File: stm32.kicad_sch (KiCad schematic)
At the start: 19 parts, among them IC1 STM32L051C6T6, J6 702472054, SW1 PTS 647 SN50 SMTR2 LFS, SW2 SW_SPDT, Y1 8MHz, Y2 ABS25-32.768KHZ-6-T

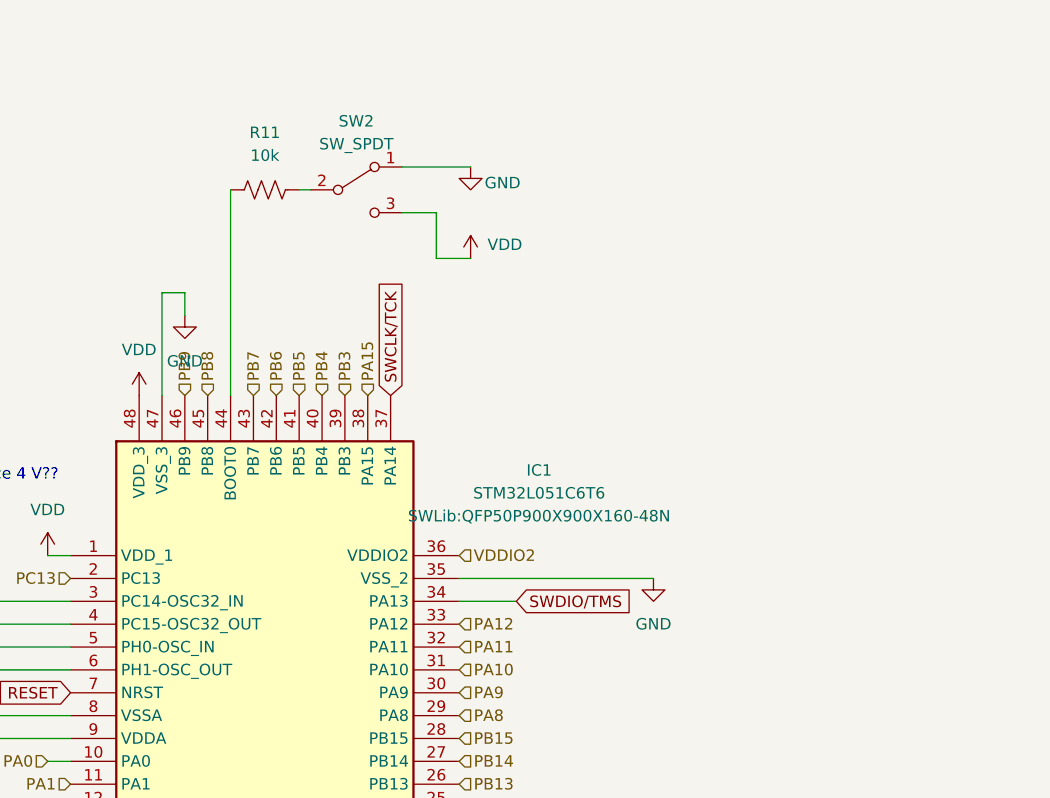
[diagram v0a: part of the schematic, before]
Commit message: removed msp430 and moved stm32, disconnected swdio and swclk in subsheet
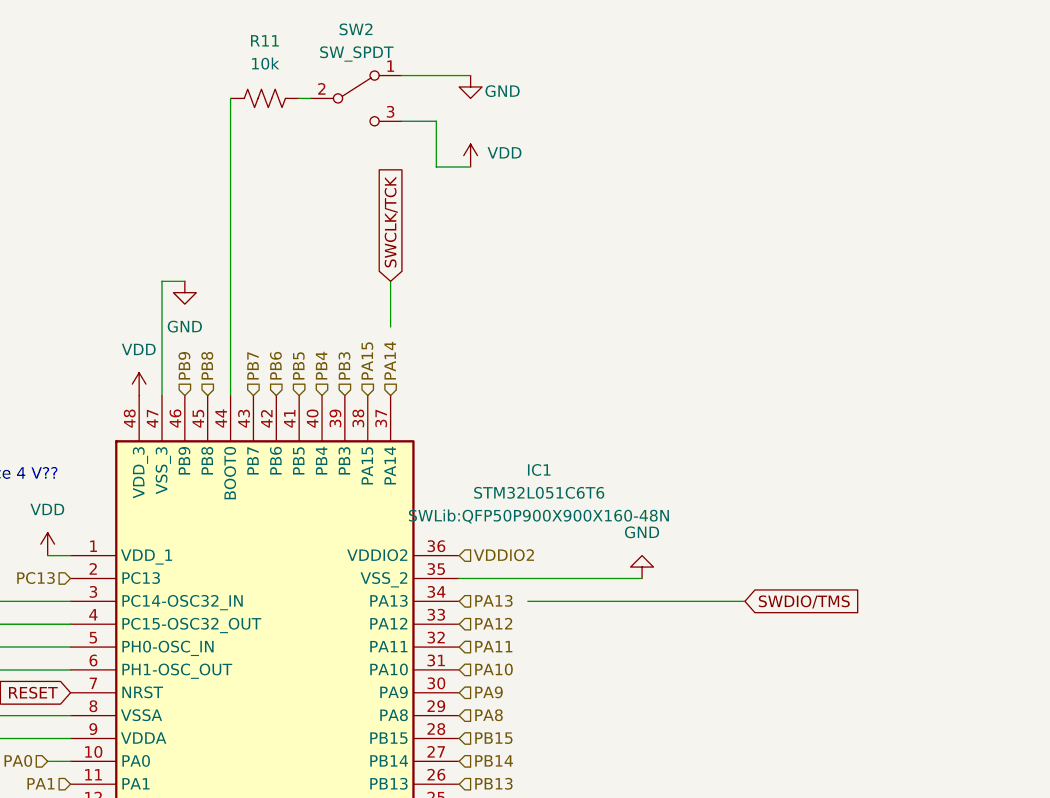
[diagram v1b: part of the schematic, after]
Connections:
- net SWCLK/TCK: no longer IC1.37 (PA14)
- net SWDIO/TMS: no longer IC1.34 (PA13)
- new net PA13: IC1.34 (PA13)
- new net PA14: IC1.37 (PA14)
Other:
- moved on the sheet: R11, SW2
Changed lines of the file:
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@@
 	(wire
 		(pts
-			(xy 147.32 44.45) (xy 149.86 44.45)
+			(xy 147.32 43.18) (xy 149.86 43.18)
 		)
 		(stroke
@@
 	(wire
 		(pts
+			(xy 172.72 43.18) (xy 172.72 48.26)
+		)
+		(stroke
+			(width 0)
+			(type default)
+		)
+	)
+	(wire
+		(pts
 			(xy 107.95 142.24) (xy 107.95 137.16)
 		)
@@
 	(wire
 		(pts
+			(xy 187.96 78.74) (xy 212.09 78.74)
+		)
+		(stroke
+			(width 0)
+			(type default)
+		)
+	)
+	(wire
+		(pts
 			(xy 105.41 149.86) (xy 105.41 154.94)
 		)
@@
 	(wire
 		(pts
-			(xy 154.94 33.02) (xy 154.94 55.88)
+			(xy 154.94 22.86) (xy 154.94 55.88)
 		)
 		(stroke
@@
 	(wire
 		(pts
-			(xy 180.34 78.74) (xy 186.69 78.74)
+			(xy 200.66 76.2) (xy 180.34 76.2)
 		)
 		(stroke
@@
 	(wire
 		(pts
-			(xy 147.32 55.88) (xy 147.32 44.45)
+			(xy 147.32 55.88) (xy 147.32 43.18)
 		)
 		(stroke
@@
 	(wire
 		(pts
-			(xy 177.8 40.64) (xy 181.61 40.64)
+			(xy 177.8 30.48) (xy 181.61 30.48)
 		)
 		(stroke
@@
 	(wire
 		(pts
-			(xy 173.99 30.48) (xy 181.61 30.48)
+			(xy 173.99 20.32) (xy 181.61 20.32)
 		)
 		(stroke
@@
 	(wire
 		(pts
-			(xy 177.8 35.56) (xy 173.99 35.56)
+			(xy 177.8 25.4) (xy 173.99 25.4)
 		)
 		(stroke
@@
 	(wire
 		(pts
-			(xy 162.56 33.02) (xy 163.83 33.02)
+			(xy 162.56 22.86) (xy 163.83 22.86)
 		)
 		(stroke
@@
 	(wire
 		(pts
-			(xy 180.34 76.2) (xy 201.93 76.2)
-		)
-		(stroke
-			(width 0)
-			(type default)
-		)
-	)
-	(wire
-		(pts
-			(xy 177.8 40.64) (xy 177.8 35.56)
+			(xy 177.8 30.48) (xy 177.8 25.4)
 		)
 		(stroke
@@
 	(wire
 		(pts
-			(xy 149.86 44.45) (xy 149.86 46.99)
-		)
-		(stroke
-			(width 0)
-			(type default)
-		)
-	)
-	(wire
-		(pts
 			(xy 127 96.52) (xy 127 91.44)
 		)
@@
 	(global_label "SWCLK{slash}TCK"
 		(shape input)
-		(at 172.72 55.88 90)
+		(at 172.72 43.18 90)
 		(fields_autoplaced yes)
 		(effects
@@
 		)
 		(property "Intersheetrefs" "${INTERSHEET_REFS}"
-			(at 172.72 41.8277 90)
+			(at 172.72 29.1277 90)
 			(effects
 				(font
@@
 	(global_label "SWDIO{slash}TMS"
 		(shape input)
-		(at 186.69 78.74 0)
+		(at 212.09 78.74 0)
 		(fields_autoplaced yes)
 		(effects
@@
 		)
 		(property "Intersheetrefs" "${INTERSHEET_REFS}"
-			(at 200.5004 78.74 0)
+			(at 225.9004 78.74 0)
 			(effects
 				(font
@@
 		)
 	)
+	(hierarchical_label "PA13"
+		(shape input)
+		(at 180.34 78.74 0)
+		(effects
+			(font
+				(size 1.27 1.27)
+			)
+			(justify left)
+		)
+	)
 	(hierarchical_label "PA11"
 		(shape input)
@@
 		)
 	)
+	(hierarchical_label "PA14"
+		(shape input)
+		(at 172.72 55.88 90)
+		(effects
+			(font
+				(size 1.27 1.27)
+			)
+			(justify left)
+		)
+	)
 	(hierarchical_label "PB4"
 		(shape input)
@@
 	(symbol
 		(lib_id "power:GND")
-		(at 149.86 46.99 0)
+		(at 149.86 43.18 0)
 		(unit 1)
 		(exclude_from_sim no)
@@
 		(fields_autoplaced yes)
 		(property "Reference" "#PWR013"
-			(at 149.86 53.34 0)
+			(at 149.86 49.53 0)
 			(effects
 				(font
@@
 		)
 		(property "Value" "GND"
-			(at 149.86 52.07 0)
+			(at 149.86 48.26 0)
 			(effects
 				(font
@@
 		)
 		(property "Footprint" ""
-			(at 149.86 46.99 0)
+			(at 149.86 43.18 0)
 			(effects
 				(font
@@
 		)
 		(property "Datasheet" "~"
-			(at 149.86 46.99 0)
+			(at 149.86 43.18 0)
 			(effects
 				(font
@@
 		)
 		(property "Description" "Power symbol creates a global label with name \"GND\" , ground"
-			(at 149.86 46.99 0)
+			(at 149.86 43.18 0)
 			(effects
 				(font
@@
 	(symbol
 		(lib_id "power:GND")
-		(at 201.93 76.2 0)
+		(at 200.66 76.2 180)
 		(unit 1)
 		(exclude_from_sim no)
@@
 		(fields_autoplaced yes)
 		(property "Reference" "#PWR019"
-			(at 201.93 82.55 0)
+			(at 200.66 69.85 0)
 			(effects
 				(font
@@
 		)
 		(property "Value" "GND"
-			(at 201.93 81.28 0)
+			(at 200.66 71.12 0)
 			(effects
 				(font
@@
 		)
 		(property "Footprint" ""
-			(at 201.93 76.2 0)
+			(at 200.66 76.2 0)
 			(effects
 				(font
@@
 		)
 		(property "Datasheet" "~"
-			(at 201.93 76.2 0)
+			(at 200.66 76.2 0)
 			(effects
 				(font
@@
 		)
 		(property "Description" "Power symbol creates a global label with name \"GND\" , ground"
-			(at 201.93 76.2 0)
+			(at 200.66 76.2 0)
 			(effects
 				(font
@@
 	(symbol
 		(lib_id "Switch:SW_SPDT")
-		(at 168.91 33.02 0)
+		(at 168.91 22.86 0)
 		(unit 1)
 		(exclude_from_sim no)
@@
 		(fields_autoplaced yes)
 		(property "Reference" "SW2"
-			(at 168.91 25.4 0)
+			(at 168.91 15.24 0)
 			(effects
 				(font
@@
 		)
 		(property "Value" "SW_SPDT"
-			(at 168.91 27.94 0)
+			(at 168.91 17.78 0)
 			(effects
 				(font
@@
 		)
 		(property "Footprint" "Button_Switch_SMD:SW_SPDT_PCM12"
-			(at 168.91 33.02 0)
+			(at 168.91 22.86 0)
 			(effects
 				(font
@@
 		)
 		(property "Datasheet" "~"
-			(at 168.91 33.02 0)
+			(at 168.91 22.86 0)
 			(effects
 				(font
@@
 		)
 		(property "Description" ""
-			(at 168.91 33.02 0)
+			(at 168.91 22.86 0)
 			(effects
 				(font
@@
 	(symbol
 		(lib_id "Device:R_US")
-		(at 158.75 33.02 90)
+		(at 158.75 22.86 90)
 		(unit 1)
 		(exclude_from_sim no)
@@
 		(fields_autoplaced yes)
 		(property "Reference" "R11"
-			(at 158.75 26.67 90)
+			(at 158.75 16.51 90)
 			(effects
 				(font
@@
 		)
 		(property "Value" "10k"
-			(at 158.75 29.21 90)
+			(at 158.75 19.05 90)
 			(effects
 				(font
@@
 		)
 		(property "Footprint" "Resistor_SMD:R_0603_1608Metric_Pad0.98x0.95mm_HandSolder"
-			(at 159.004 32.004 90)
+			(at 159.004 21.844 90)
 			(effects
 				(font
@@
 		)
 		(property "Datasheet" "~"
-			(at 158.75 33.02 0)
+			(at 158.75 22.86 0)
 			(effects
 				(font
@@
 		)
 		(property "Description" ""
-			(at 158.75 33.02 0)
+			(at 158.75 22.86 0)
 			(effects
 				(font
@@
 	(symbol
 		(lib_id "power:VDD")
-		(at 181.61 40.64 0)
+		(at 181.61 30.48 0)
 		(unit 1)
 		(exclude_from_sim no)
@@
 		(dnp no)
 		(property "Reference" "#PWR017"
-			(at 181.61 44.45 0)
+			(at 181.61 34.29 0)
 			(effects
 				(font
@@
 		)
 		(property "Value" "VDD"
-			(at 185.42 39.116 0)
+			(at 185.42 28.956 0)
 			(effects
 				(font
@@
 		)
 		(property "Footprint" ""
-			(at 181.61 40.64 0)
+			(at 181.61 30.48 0)
 			(effects
 				(font
@@
 		)
 		(property "Datasheet" ""
-			(at 181.61 40.64 0)
+			(at 181.61 30.48 0)
 			(effects
 				(font
@@
 		)
 		(property "Description" ""
-			(at 181.61 40.64 0)
+			(at 181.61 30.48 0)
 			(effects
 				(font
@@
 	(symbol
 		(lib_id "power:GND")
-		(at 181.61 30.48 0)
+		(at 181.61 20.32 0)
 		(unit 1)
 		(exclude_from_sim no)
@@
 		(dnp no)
 		(property "Reference" "#PWR016"
-			(at 181.61 36.83 0)
+			(at 181.61 26.67 0)
 			(effects
 				(font
@@
 		)
 		(property "Value" "GND"
-			(at 185.166 32.258 0)
+			(at 185.166 22.098 0)
 			(effects
 				(font
@@
 		)
 		(property "Footprint" ""
-			(at 181.61 30.48 0)
+			(at 181.61 20.32 0)
 			(effects
 				(font
@@
 		)
 		(property "Datasheet" "~"
-			(at 181.61 30.48 0)
+			(at 181.61 20.32 0)
 			(effects
 				(font
@@
 		)
 		(property "Description" "Power symbol creates a global label with name \"GND\" , ground"
-			(at 181.61 30.48 0)
+			(at 181.61 20.32 0)
 			(effects
 				(font
